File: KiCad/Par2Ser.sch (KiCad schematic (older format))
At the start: 33 parts, among them J1 DB25_Male, J2 USB_C_Receptacle_USB2.0, U1 LC4032V-5TN48C, U2 FT240XS-R

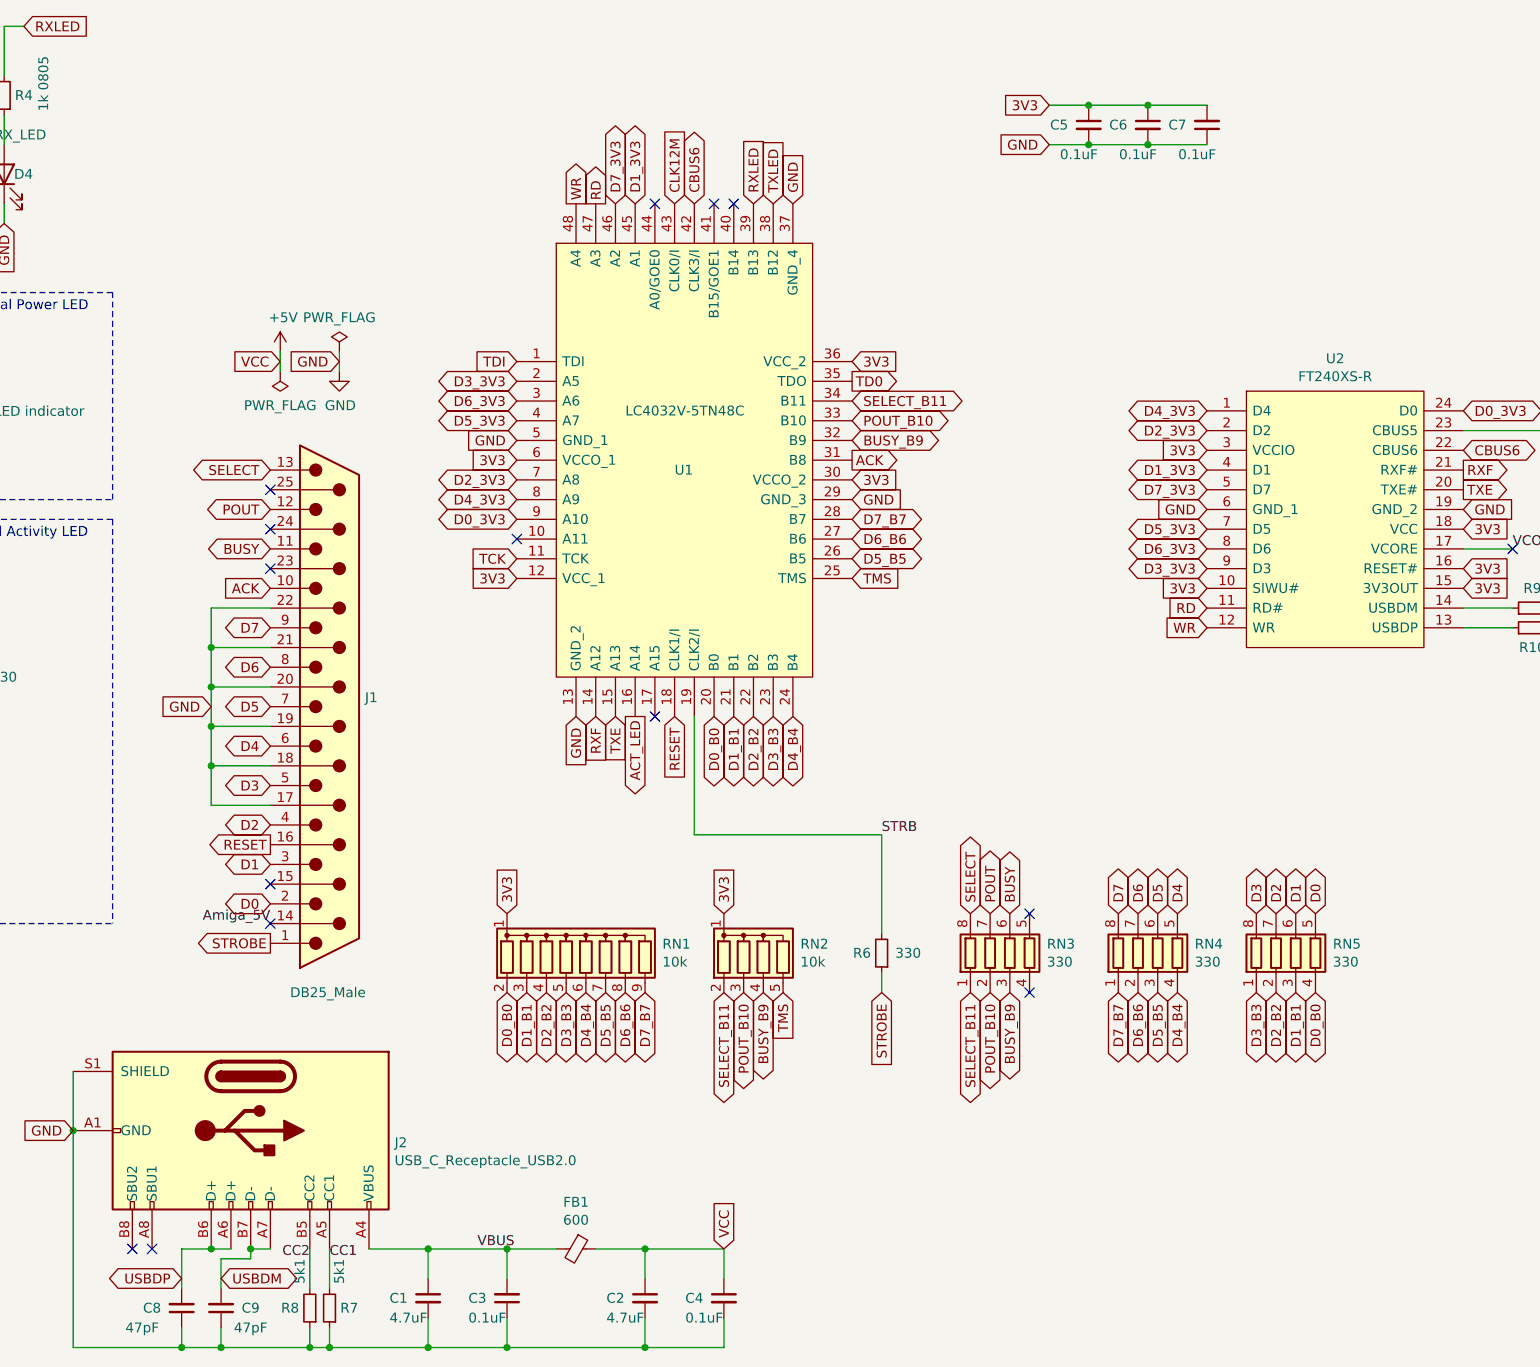
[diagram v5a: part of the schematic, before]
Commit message: Add remaining caps on 3V3 pins for CPLD and route power traces
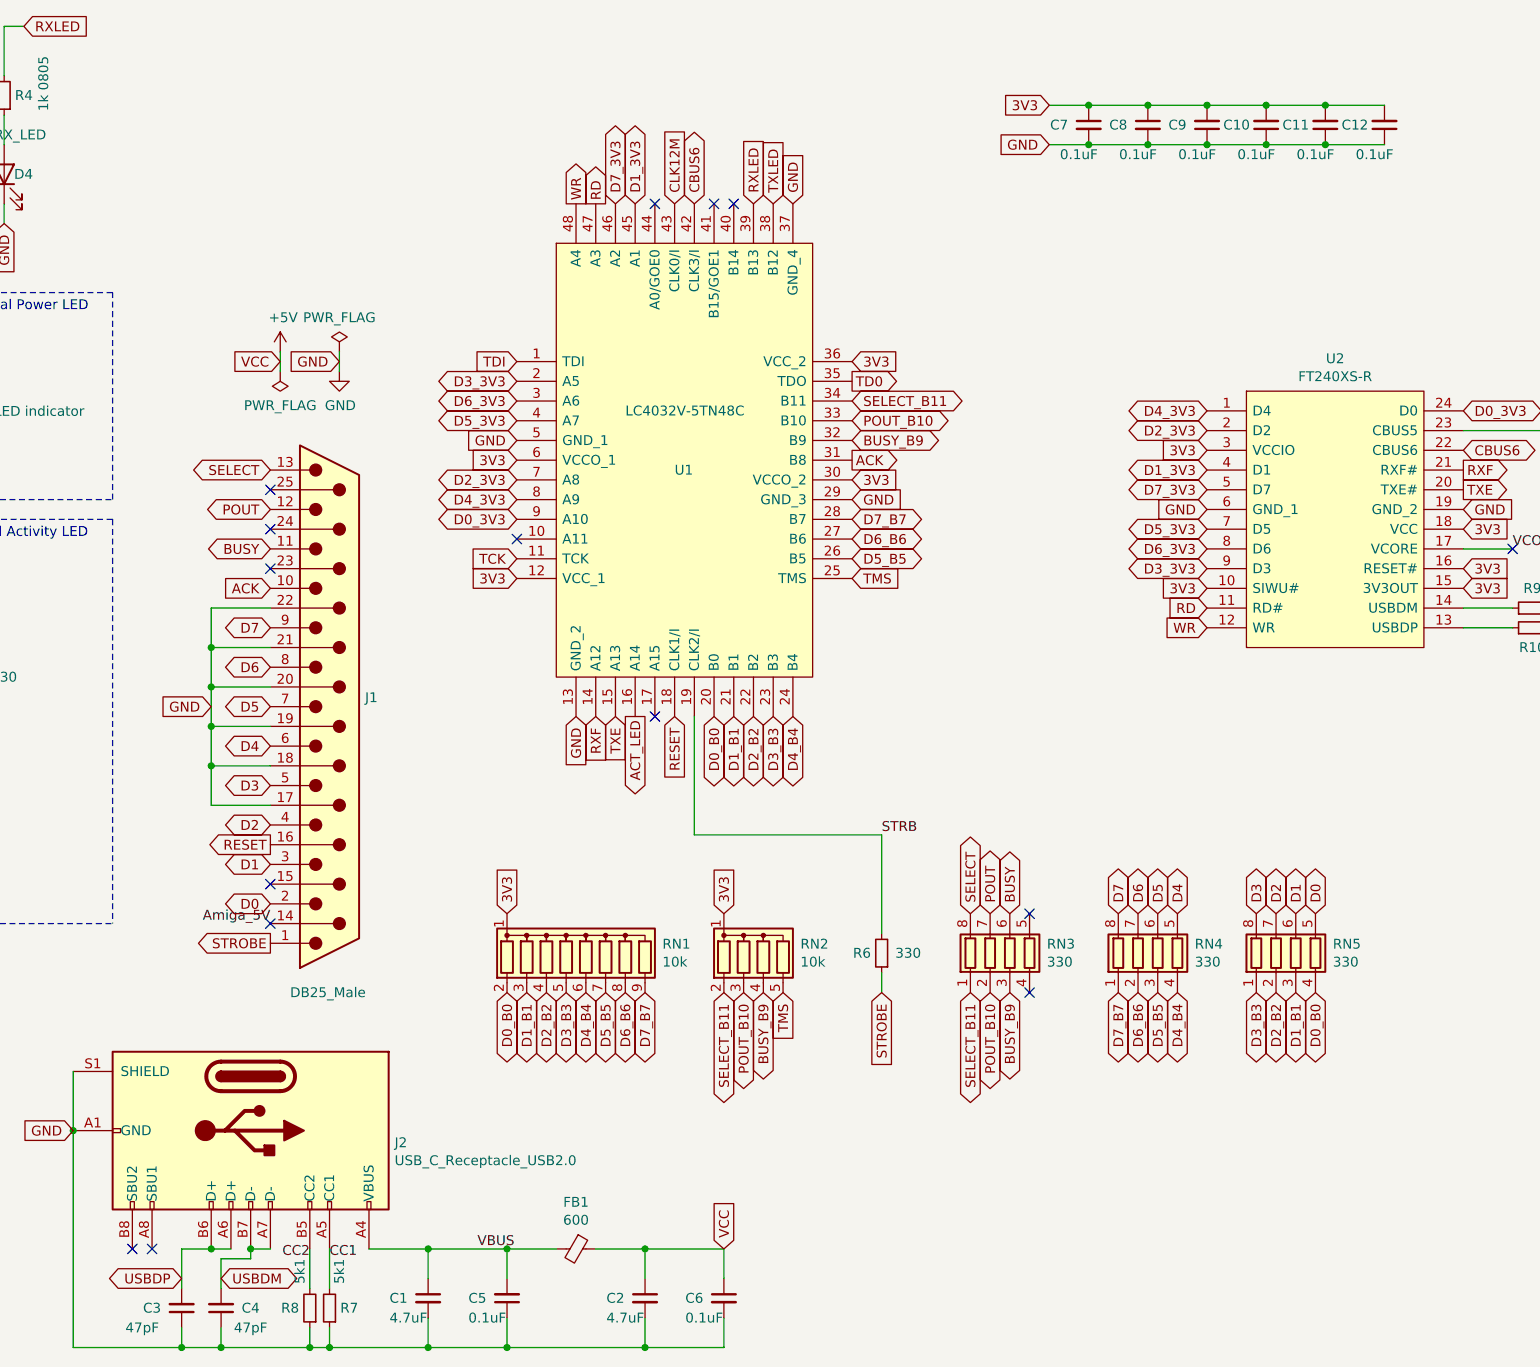
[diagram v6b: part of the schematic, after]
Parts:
- added C10, C11, C12: 0.1uF, Capacitor_SMD:C_0603_1608Metric_Pad1.08x0.95mm_HandSolder, symbol Device:C_Small
- renumbered C8 to C3, C9 to C4, C3 to C5, C4 to C6, C5 to C7, C6 to C8, C7 to C9
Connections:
- net 3V3: now also C10.2, C11.2, C12.2
- net GND: now also C10.1, C11.1, C12.1
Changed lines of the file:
@@
 $EndComp
 $Comp
-L Device:C_Small C7
+L Device:C_Small C9
 U 1 1 611D1D5F
 P 8500 1250
-F 0 "C7" H 8650 1250 50  0000 C CNN
+F 0 "C9" H 8650 1250 50  0000 C CNN
 F 1 "0.1uF" H 8550 1400 50  0000 C CNN
 F 2 "Capacitor_SMD:C_0603_1608Metric_Pad1.08x0.95mm_HandSolder" H 8500 1250 50  0001 C CNN
@@
 $EndComp
 $Comp
-L Device:C_Small C5
+L Device:C_Small C7
 U 1 1 612089E2
 P 7900 1250
-F 0 "C5" H 7750 1250 50  0000 C CNN
+F 0 "C7" H 7750 1250 50  0000 C CNN
 F 1 "0.1uF" H 7850 1100 50  0000 C CNN
 F 2 "Capacitor_SMD:C_0805_2012Metric_Pad1.18x1.45mm_HandSolder" H 7900 1250 50  0001 C CNN
@@
 Amiga_5V
 $Comp
-L Device:C_Small C4
+L Device:C_Small C6
 U 1 1 67141D33
 P 6050 7200
-F 0 "C4" H 5900 7200 50  0000 C CNN
+F 0 "C6" H 5900 7200 50  0000 C CNN
 F 1 "0.1uF" H 5950 7100 50  0000 C CNN
 F 2 "Capacitor_SMD:C_0805_2012Metric_Pad1.18x1.45mm_HandSolder" H 6050 7200 50  0001 C CNN
@@
 GND
 $Comp
-L Device:C_Small C3
+L Device:C_Small C5
 U 1 1 67247829
 P 4950 7200
-F 0 "C3" H 5100 7200 50  0000 C CNN
+F 0 "C5" H 5100 7200 50  0000 C CNN
 F 1 "0.1uF" H 5050 7300 50  0000 C CNN
 F 2 "Capacitor_SMD:C_0805_2012Metric_Pad1.18x1.45mm_HandSolder" H 4950 7200 50  0001 C CNN
@@
 	3500 7450 3300 7450
 $Comp
-L Device:C_Small C8
+L Device:C_Small C3
 U 1 1 671F8752
 P 3300 7250
-F 0 "C8" H 3450 7250 50  0000 C CNN
+F 0 "C3" H 3450 7250 50  0000 C CNN
 F 1 "47pF" H 3500 7350 50  0000 C CNN
 F 2 "Capacitor_SMD:C_0603_1608Metric_Pad1.08x0.95mm_HandSolder" H 3300 7250 50  0001 C CNN
@@
 $EndComp
 $Comp
-L Device:C_Small C9
+L Device:C_Small C4
 U 1 1 671FEDD5
 P 3500 7250
-F 0 "C9" H 3350 7250 50  0000 C CNN
+F 0 "C4" H 3350 7250 50  0000 C CNN
 F 1 "47pF" H 3350 7350 50  0000 C CNN
 F 2 "Capacitor_SMD:C_0603_1608Metric_Pad1.08x0.95mm_HandSolder" H 3500 7250 50  0001 C CNN
@@
 STRB
 $Comp
-L Device:C_Small C6
+L Device:C_Small C8
 U 1 1 5EB53531
 P 8200 1250
-F 0 "C6" H 8050 1250 50  0000 C CNN
+F 0 "C8" H 8050 1250 50  0000 C CNN
 F 1 "0.1uF" H 8150 1100 50  0000 C CNN
 F 2 "Capacitor_SMD:C_0603_1608Metric_Pad1.08x0.95mm_HandSolder" H 8200 1250 50  0001 C CNN
@@
 Wire Wire Line
 	10450 3800 10250 3800
+$Comp
+L Device:C_Small C10
+U 1 1 6A632E26
+P 8800 1250
+F 0 "C10" H 8950 1250 50  0000 C CNN
+F 1 "0.1uF" H 8850 1400 50  0000 C CNN
+F 2 "Capacitor_SMD:C_0603_1608Metric_Pad1.08x0.95mm_HandSolder" H 8800 1250 50  0001 C CNN
+F 3 "~" H 8800 1250 50  0001 C CNN
+	1    8800 1250
+	-1   0    0    1
+$EndComp
+Wire Wire Line
+	8800 1150 8500 1150
+Connection ~ 8500 1150
+Wire Wire Line
+	8800 1350 8500 1350
+Connection ~ 8500 1350
+$Comp
+L Device:C_Small C11
+U 1 1 6A647103
+P 9100 1250
+F 0 "C11" H 9250 1250 50  0000 C CNN
+F 1 "0.1uF" H 9150 1400 50  0000 C CNN
+F 2 "Capacitor_SMD:C_0603_1608Metric_Pad1.08x0.95mm_HandSolder" H 9100 1250 50  0001 C CNN
+F 3 "~" H 9100 1250 50  0001 C CNN
+	1    9100 1250
+	-1   0    0    1
+$EndComp
+Wire Wire Line
+	8800 1150 9100 1150
+Connection ~ 8800 1150
+Wire Wire Line
+	8800 1350 9100 1350
+Connection ~ 8800 1350
+$Comp
+L Device:C_Small C12
+U 1 1 6A67B251
+P 9400 1250
+F 0 "C12" H 9550 1250 50  0000 C CNN
+F 1 "0.1uF" H 9450 1400 50  0000 C CNN
+F 2 "Capacitor_SMD:C_0603_1608Metric_Pad1.08x0.95mm_HandSolder" H 9400 1250 50  0001 C CNN
+F 3 "~" H 9400 1250 50  0001 C CNN
+	1    9400 1250
+	-1   0    0    1
+$EndComp
+Wire Wire Line
+	9400 1150 9100 1150
+Connection ~ 9100 1150
+Wire Wire Line
+	9400 1350 9100 1350
+Connection ~ 9100 1350
 $EndSCHEMATC

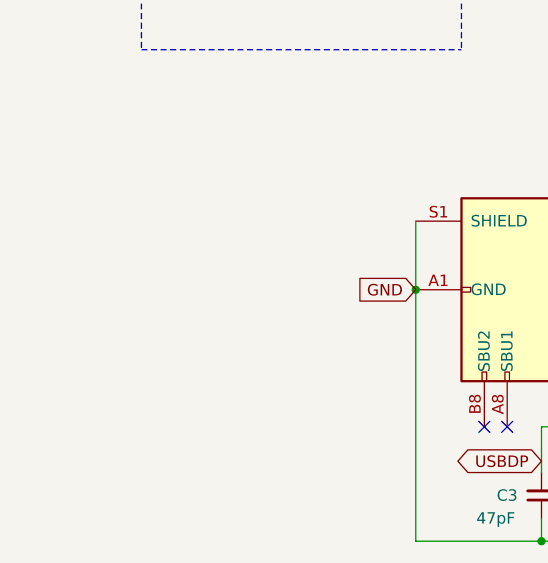
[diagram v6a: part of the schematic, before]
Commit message: Add JTAG header
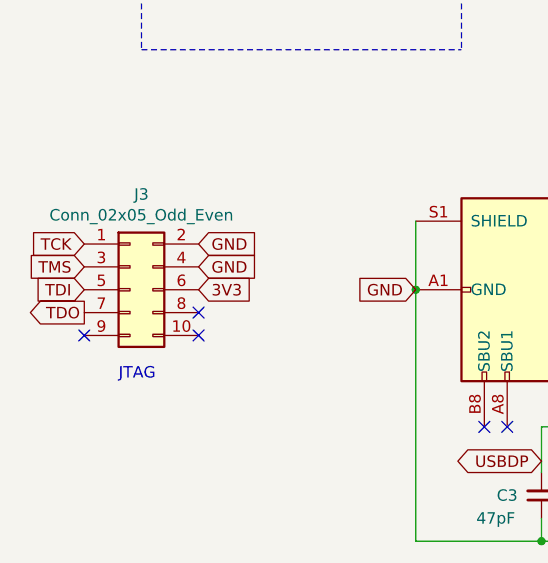
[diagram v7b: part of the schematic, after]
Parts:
- added J3: Conn_02x05_Odd_Even, Connector_PinHeader_2.54mm:PinHeader_2x05_P2.54mm_Vertical, symbol Connector_Generic:Conn_02x05_Odd_Even
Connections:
- net 3V3: now also J3.6 (Pin_6)
- net GND: now also J3.2 (Pin_2), J3.4 (Pin_4)
- net TCK: now also J3.1 (Pin_1)
- net TDI: now also J3.5 (Pin_5)
- net TMS: now also J3.3 (Pin_3)
- new net TDO: J3.7 (Pin_7)
- no-connect marks 15 -> 18
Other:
- note added: "JTAG"
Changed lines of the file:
@@
 	9400 1350 9100 1350
 Connection ~ 9100 1350
+$Comp
+L Connector_Generic:Conn_02x05_Odd_Even J3
+U 1 1 6A69D469
+P 1500 6350
+F 0 "J3" H 1550 6767 50  0000 C CNN
+F 1 "Conn_02x05_Odd_Even" H 1550 6676 50  0000 C CNN
+F 2 "Connector_PinHeader_2.54mm:PinHeader_2x05_P2.54mm_Vertical" H 1500 6350 50  0001 C CNN
+F 3 "~" H 1500 6350 50  0001 C CNN
+	1    1500 6350
+	1    0    0    -1
+$EndComp
+Text GLabel 1300 6150 0    50   Input ~ 0
+TCK
+Text GLabel 1300 6250 0    50   Input ~ 0
+TMS
+Text GLabel 1300 6350 0    50   Input ~ 0
+TDI
+Text GLabel 1300 6450 0    50   Output ~ 0
+TDO
+NoConn ~ 1300 6550
+NoConn ~ 1800 6550
+NoConn ~ 1800 6450
+Text GLabel 1800 6150 2    50   Input ~ 0
+GND
+Text GLabel 1800 6250 2    50   Input ~ 0
+GND
+Text GLabel 1800 6350 2    50   Input ~ 0
+3V3
+Text Notes 1450 6750 0    50   ~ 0
+JTAG
 $EndSCHEMATC
